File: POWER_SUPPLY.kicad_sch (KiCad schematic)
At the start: 53 parts, among them J1 Jack-DC, Q1 NTJD4401NT1G, Q2 NTJD4401NT1G, Q3 NTJD4401NT1G, U5 LM66100DCK, U6 LMR33640ADDA, U7 LMR33640ADDA

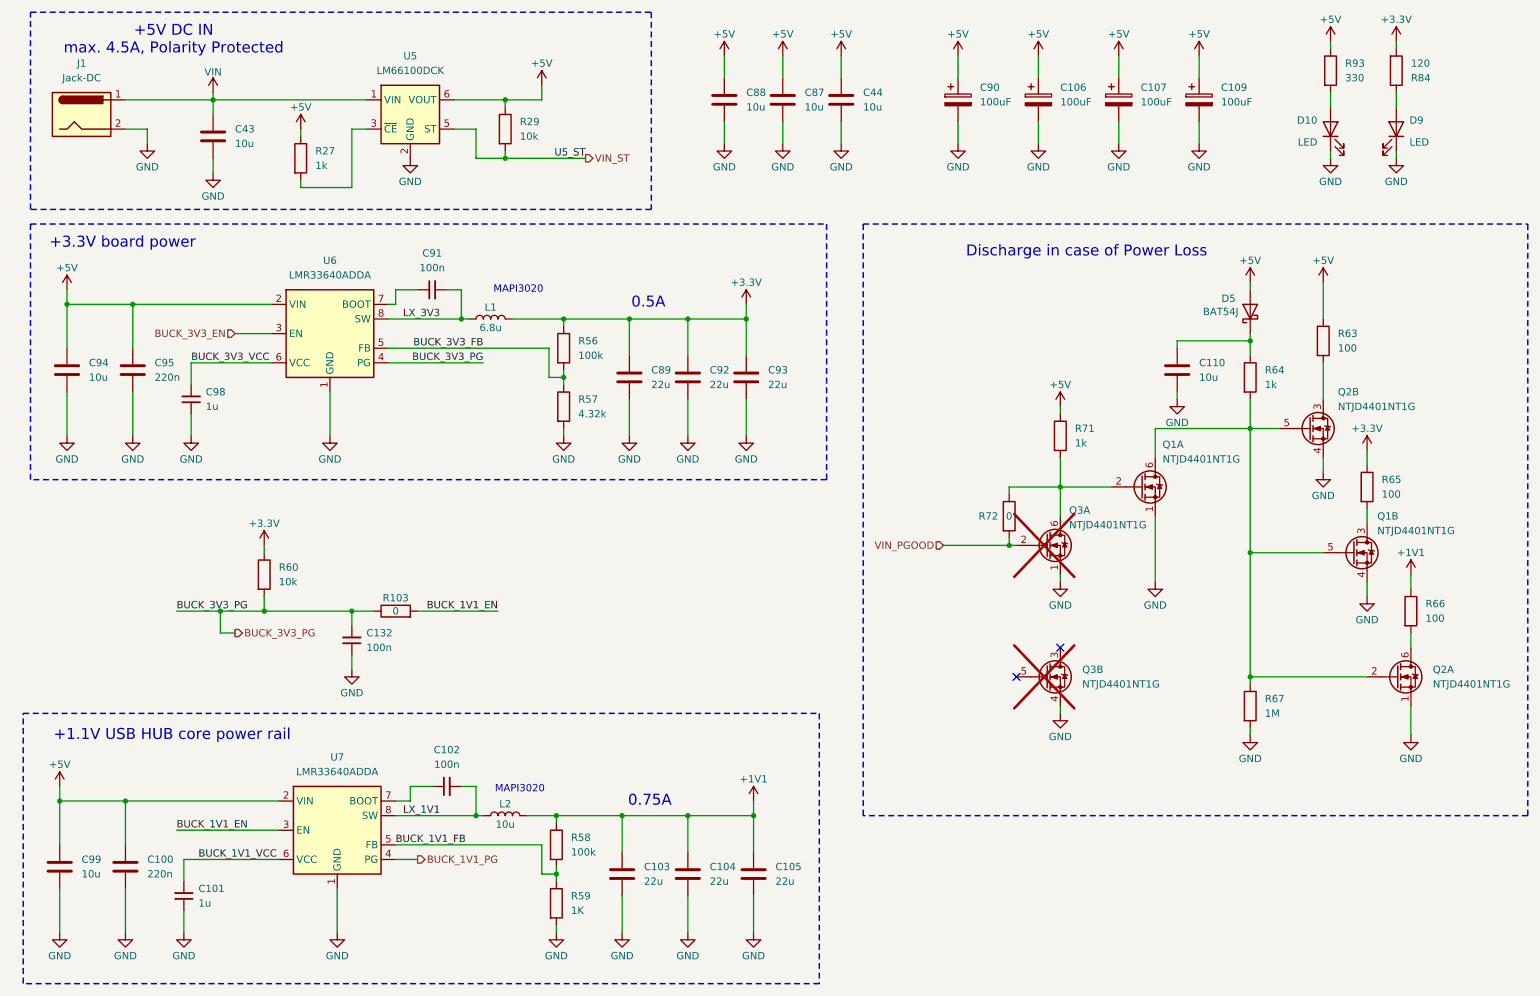
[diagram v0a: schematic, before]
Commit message: Power In Circuitry extended for more current
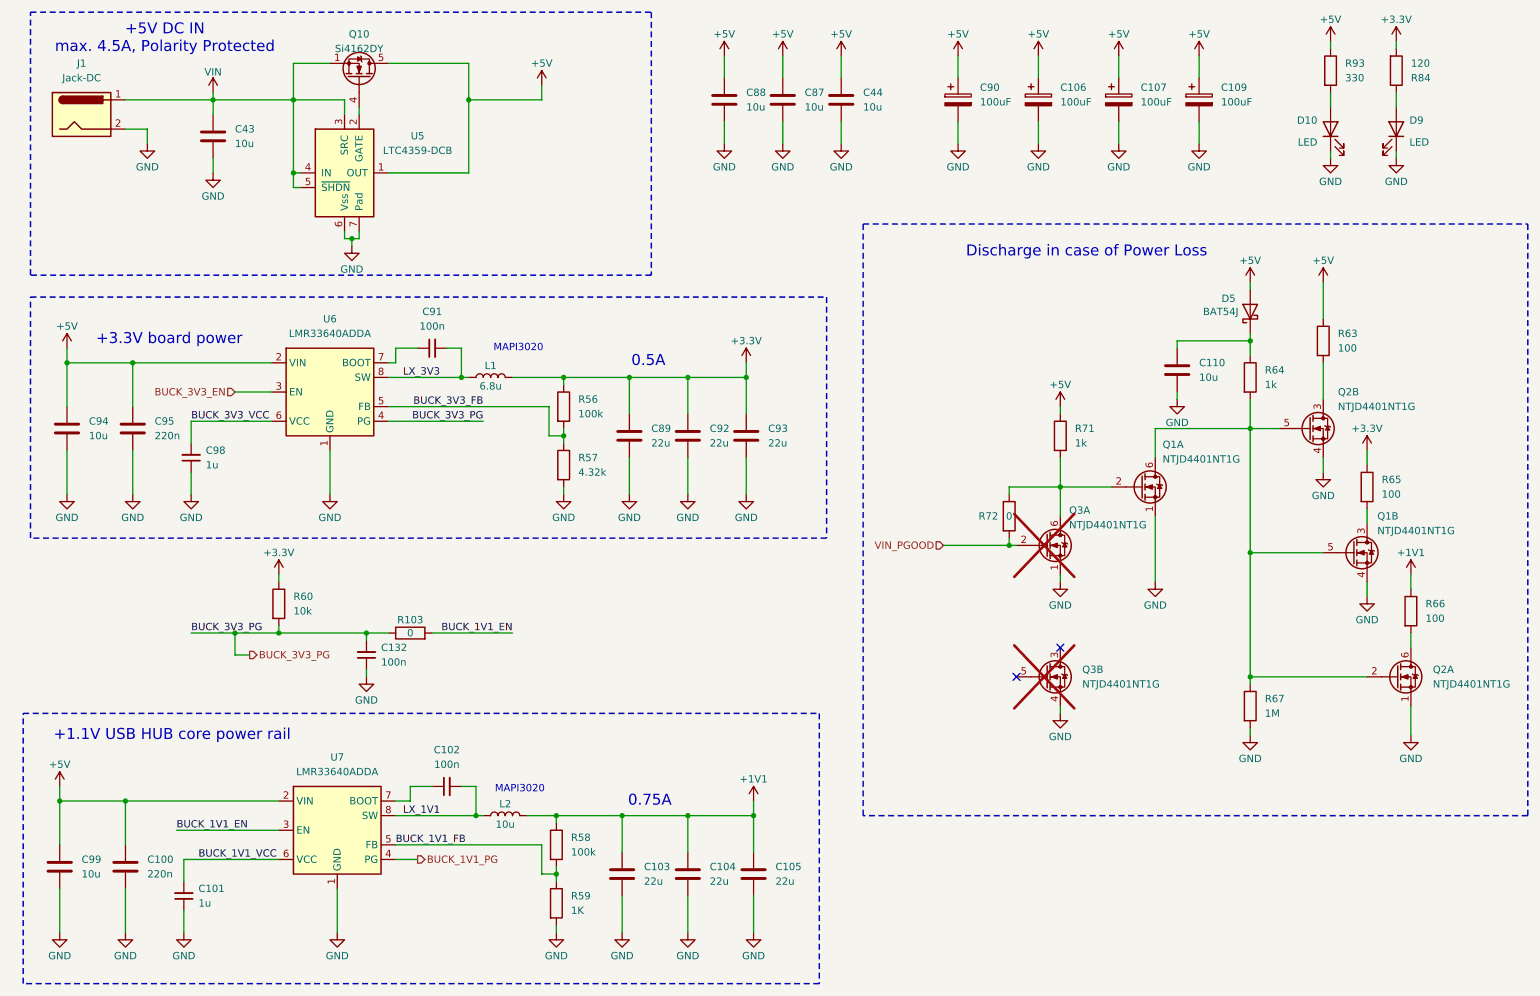
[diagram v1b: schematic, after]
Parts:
- removed R27: 1k, 00_Resistor:Res_0402, symbol Device:R
- removed R29: 10k, 00_Resistor:Res_0402, symbol Device:R
- removed U5: LM66100DCK, Package_TO_SOT_SMD:SOT-363_SC-70-6, symbol Power_Management:LM66100DCK
- added Q10: Si4162DY, Package_SO:SOIC-8_3.9x4.9mm_P1.27mm, symbol Transistor_FET:Si4162DY
- added U5: LTC4359-DCB, Package_DFN_QFN:DFN-6-1EP_3x2mm_P0.5mm_EP1.65x1.35mm, symbol Power_Management:LTC4359-DCB
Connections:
- net +5V: now also Q10.5 (D), Q10.6 (D), Q10.7 (D), Q10.8 (D), U5.1 (OUT)
- net GND: now also U5.6 (Vss), U5.7 (Pad)
- net VIN: now also Q10.1 (S), Q10.2 (S), Q10.3 (S), U5.3 (SRC), U5.4 (IN), U5.5 (~{SHDN})
- new net: Q10.4 (G), U5.2 (GATE)
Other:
- moved on the sheet: C132, C89, C91, C92, C93, C94, C95, C98, L1, R103, R56, R57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
